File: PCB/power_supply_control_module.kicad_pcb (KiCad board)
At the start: 2 copper layers, 3 parts, among them SW3 RotaryEncoder, SW4 RotaryEncoder, U1 ATmega328P-A

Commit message: schematic and board WIP
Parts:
- added C1: 100nF, Capacitor_SMD:C_1206_3216Metric_Pad1.33x1.80mm_HandSolder, F.Cu at (142.0, 87.2)
- added C2: 1uF, Capacitor_SMD:C_1206_3216Metric_Pad1.33x1.80mm_HandSolder, F.Cu at (142.0, 84.8)
- added C3: 10uF, Capacitor_SMD:C_1206_3216Metric_Pad1.33x1.80mm_HandSolder, F.Cu at (142.0, 82.3)
- added C4: 22pF, Capacitor_SMD:C_1206_3216Metric_Pad1.33x1.80mm_HandSolder, F.Cu at (143.5, 104.2)
- added C5: 22pF, Capacitor_SMD:C_1206_3216Metric_Pad1.33x1.80mm_HandSolder, F.Cu at (137.7, 104.2)
- added D1: Voltage, LED_SMD:LED_0603_1608Metric_Pad1.05x0.95mm_HandSolder, B.Cu at (131.8, 108.3)
- added D2: Current, LED_SMD:LED_0603_1608Metric_Pad1.05x0.95mm_HandSolder, B.Cu at (175.8, 108.3)
- added H1: MountingHole, MountingHole:MountingHole_3.2mm_M3_ISO7380, F.Cu at (125.3, 98.8)
- added H2: MountingHole, MountingHole:MountingHole_3.2mm_M3_ISO7380, F.Cu at (181.9, 98.8)
- added J1: ICSP, Connector_PinHeader_2.54mm:PinHeader_2x03_P2.54mm_Vertical, F.Cu at (152.9, 92.0)
- added J2: PS_POT, Connector_JST:JST_XH_B4B-XH-A_1x04_P2.50mm_Vertical, F.Cu at (151.2, 79.3)
- added J3: PWR+UART, Connector_PinHeader_2.54mm:PinHeader_1x04_P2.54mm_Vertical, F.Cu at (126.5, 124.4)
- added R1: 10K, Resistor_SMD:R_1206_3216Metric_Pad1.30x1.75mm_HandSolder, F.Cu at (167.4, 108.0)
- added R2: 1K, Resistor_SMD:R_1206_3216Metric_Pad1.30x1.75mm_HandSolder, B.Cu at (127.0, 107.3)
- added R3: 1K, Resistor_SMD:R_1206_3216Metric_Pad1.30x1.75mm_HandSolder, B.Cu at (182.1, 107.8)
- added R4: 1K, Resistor_SMD:R_1206_3216Metric_Pad1.30x1.75mm_HandSolder, F.Cu at (143.4, 123.8)
- added R5: 1K, Resistor_SMD:R_1206_3216Metric_Pad1.30x1.75mm_HandSolder, F.Cu at (140.5, 123.8)
- added SW1: Voltage, Button_Switch_THT:SW_TH_Tactile_Omron_B3F-107x, B.Cu at (129.6, 110.2)
- added SW2: Current, Button_Switch_THT:SW_TH_Tactile_Omron_B3F-107x, B.Cu at (173.4, 110.2)
- added U2: MCP4251-103E-SL, Package_SO:SOIC-14_3.9x8.7mm_P1.27mm, F.Cu at (170.8, 100.2)
- added Y1: Crystal, Crystal:Crystal_HC49-4H_Vertical, B.Cu at (142.8, 101.2)
- SW3: value RotaryEncoder -> Voltage; moved to B.Cu
- SW4: value RotaryEncoder -> Current; moved to B.Cu
- moved SW4 63.4 mm to (173.2, 77.3), turned to -90 degrees
- moved U1 30.9 mm to (138.3, 94.0), turned to 90 degrees
- moved SW3 23.8 mm to (129.3, 77.3), turned to -90 degrees
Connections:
- SW3 pad A: unconnected-(SW3-PadA) -> /ENC_V_A
- SW3 pad B: unconnected-(SW3-PadB) -> /ENC_V_B
- SW3 pad C: unconnected-(SW3-PadC) -> GNDD
- SW4 pad A: unconnected-(SW4-PadA) -> /ENC_A_A
- SW4 pad B: unconnected-(SW4-PadB) -> /ENC_A_B
- SW4 pad C: unconnected-(SW4-PadC) -> GNDD
- U1 pad 1: unconnected-(U1-PD3-Pad1) -> /SW_A
- U1 pad 10: unconnected-(U1-PD6-Pad10) -> /ENC_A_A
- U1 pad 11: unconnected-(U1-PD7-Pad11) -> /ENC_A_B
- U1 pad 14: unconnected-(U1-PB2-Pad14) -> /~{MCP_CS}
- U1 pad 15: unconnected-(U1-PB3-Pad15) -> /MOSI
- U1 pad 16: unconnected-(U1-PB4-Pad16) -> /MISO
- U1 pad 17: unconnected-(U1-PB5-Pad17) -> /SCK
- U1 pad 18: unconnected-(U1-AVCC-Pad18) -> VCC
- U1 pad 2: unconnected-(U1-PD4-Pad2) -> /ENC_V_A
- U1 pad 21: Net-(U1-GND-Pad21) -> GNDD
- U1 pad 25: unconnected-(U1-PC2-Pad25) -> /LED_V
- U1 pad 26: unconnected-(U1-PC3-Pad26) -> /LED_A
- U1 pad 29: unconnected-(U1-~{RESET}/PC6-Pad29) -> /RST
- U1 pad 3: Net-(U1-GND-Pad21) -> GNDD
- U1 pad 30: unconnected-(U1-PD0-Pad30) -> /RXD0
- U1 pad 31: unconnected-(U1-PD1-Pad31) -> /TXD0
- U1 pad 32: unconnected-(U1-PD2-Pad32) -> /SW_V
- U1 pad 4: Net-(U1-VCC-Pad4) -> VCC
- U1 pad 5: Net-(U1-GND-Pad21) -> GNDD
- U1 pad 6: Net-(U1-VCC-Pad4) -> VCC
- U1 pad 7: unconnected-(U1-XTAL1/PB6-Pad7) -> Net-(U1-XTAL1/PB6)
- U1 pad 8: unconnected-(U1-XTAL2/PB7-Pad8) -> Net-(U1-XTAL2/PB7)
- U1 pad 9: unconnected-(U1-PD5-Pad9) -> /ENC_V_B
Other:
- board outline added: 64.3 x 55 mm

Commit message: second MCP added WIP
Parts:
- added R10: 10K, Resistor_SMD:R_1206_3216Metric_Pad1.30x1.75mm_HandSolder, F.Cu at (166.7, 124.4)
- added R11: 10K, Resistor_SMD:R_1206_3216Metric_Pad1.30x1.75mm_HandSolder, F.Cu at (166.7, 127.7)
- added R4: 2k, Resistor_SMD:R_1206_3216Metric_Pad1.30x1.75mm_HandSolder, F.Cu at (163.8, 108.0)
- added R7: 10K, Resistor_SMD:R_1206_3216Metric_Pad1.30x1.75mm_HandSolder, F.Cu at (165.2, 113.3)
- added R8: 10K, Resistor_SMD:R_1206_3216Metric_Pad1.30x1.75mm_HandSolder, F.Cu at (166.7, 117.8)
- added R9: 10K, Resistor_SMD:R_1206_3216Metric_Pad1.30x1.75mm_HandSolder, F.Cu at (166.7, 121.1)
- added U3: MCP4251-103E-SL, Package_SO:SOIC-14_3.9x8.7mm_P1.27mm, F.Cu at (177.8, 122.8)
- renumbered R4 to R5, R5 to R6
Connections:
- net /~{MCP_CS} renamed /~{MCP_CS1}
- U1 pad 13: unconnected-(U1-PB1-Pad13) -> /~{MCP_CS2}
- U2 pad 7: /_VCC -> Net-(U2-P1A)

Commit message: Schematic finished
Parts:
- added C4: 100nF, Capacitor_SMD:C_1206_3216Metric_Pad1.33x1.80mm_HandSolder, F.Cu at (171.7, 100.3)
- added C7: 100nF, Capacitor_SMD:C_1206_3216Metric_Pad1.33x1.80mm_HandSolder, F.Cu at (171.7, 103.7)
- moved R4 11.9 mm to (138.1, 111.5)
- moved R8 9.91 mm to (130.6, 124.2)
- moved R7 8.60 mm to (134.8, 123.8)
- moved U3 6.15 mm to (170.6, 94.1)
- moved J2 3.79 mm to (124.5, 121.2), turned to 180 degrees
- renumbered C4 to C5, C5 to C6, J3 to J2, J2 to J3, R7 to R1, R11 to R10, R10 to R11, R8 to R2, R4 to R3, R2 to R4, R3 to R5, R9 to R6, R5 to R7, R6 to R8, R1 to R9, U3 to U1, U1 to U2, U2 to U3
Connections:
- net /ENC_A_A renamed /ENC_C_A
- net /ENC_A_B renamed /ENC_C_B
- net /LED_A renamed /LED_C
- net /SW_A renamed /SW_C
- net /_POT_A renamed /_POT_C
- J3 pad 3: /_GND -> GND2
- J3 pad 4: /_VCC -> VCC2
- R1 pad 1: /~{MCP_CS1} -> /~{MCP_CS2}
- R10 pad 1: unconnected-(R11-Pad1) -> Net-(U1-P0B)
- R10 pad 2: unconnected-(R11-Pad2) -> GND2
- R11 pad 1: unconnected-(R10-Pad1) -> GND2
- R11 pad 2: unconnected-(R10-Pad2) -> Net-(U1-P1B)
- R2 pad 1: unconnected-(R8-Pad1) -> Net-(U1-P0B)
- R2 pad 2: unconnected-(R8-Pad2) -> VCC2
- R3 pad 1: /_VCC -> VCC2
- R3 pad 2: Net-(U2-P1A) -> Net-(U1-P1A)
- R6 pad 1: unconnected-(R9-Pad1) -> Net-(U1-P1B)
- R6 pad 2: unconnected-(R9-Pad2) -> Net-(U1-P1A)
- U1 pad 1: /~{MCP_CS1} -> /~{MCP_CS2}
- U1 pad 10: unconnected-(U3-P0B-Pad10) -> Net-(U1-P0B)
- U1 pad 5: unconnected-(U3-P1B-Pad5) -> Net-(U1-P1B)
- U1 pad 6: unconnected-(U3-P1W-Pad6) -> Net-(U1-P1B)
- U1 pad 7: unconnected-(U3-P1A-Pad7) -> Net-(U1-P1A)
- U1 pad 8: unconnected-(U3-P0A-Pad8) -> VCC2
- U1 pad 9: unconnected-(U3-P0W-Pad9) -> Net-(U1-P0B)
- U3 pad 10: /_GND -> GND2
- U3 pad 5: /_GND -> GND2
- U3 pad 7: Net-(U2-P1A) -> Net-(U1-P1B)
- U3 pad 8: /_VCC -> Net-(U1-P0B)

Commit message: PCB WIP
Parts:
- R4: moved to F.Cu
- moved R10 24.0 mm to (173.8, 104.8), turned to 180 degrees
- moved R6 21.4 mm to (152.8, 104.8)
- moved R3 21.2 mm to (183.5, 115.8)
- moved C7 20.9 mm to (175.7, 124.2), turned to 90 degrees
- moved R7 20.2 mm to (123.3, 107.2), turned to -90 degrees
- moved R9 18.7 mm to (173.7, 90.4), turned to 0 degrees
- moved R11 18.6 mm to (173.8, 107.2), turned to 180 degrees
- moved R8 17.4 mm to (126.5, 107.2)
- moved R1 17.0 mm to (178.4, 124.2), turned to -90 degrees
- moved R2 15.8 mm to (152.4, 111.0)
- moved C2 8.97 mm to (133.7, 88.2), turned to 180 degrees
- moved U1 8.36 mm to (169.5, 124.0), turned to -90 degrees
- moved C4 7.64 mm to (173.7, 92.9), turned to 180 degrees
- moved J1 6.23 mm to (147.8, 88.5)
- moved U3 5.71 mm to (173.7, 98.9), turned to 0 degrees
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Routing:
- net /MISO: track 0.00 -> 78.1 mm, vias 0 -> 3
- net /ENC_C_B: track 0.00 -> 67.8 mm, vias 0 -> 1
- net /SCK: track 0.00 -> 67.6 mm, vias 0 -> 3
- net /MOSI: track 0.00 -> 65.9 mm
- net /ENC_C_A: track 0.00 -> 64.5 mm, vias 0 -> 1
- net /LED_V: track 0.00 -> 57.7 mm, vias 0 -> 2
- net VCC: track 0.00 -> 56.4 mm
- net /RST: track 0.00 -> 43.5 mm
- net /ENC_V_B: track 0.00 -> 28.5 mm, vias 0 -> 2
- net /SW_C: track 0.00 -> 26.9 mm, vias 0 -> 1
- net GND2: track 0.00 -> 25.8 mm
- net /LED_C: track 0.00 -> 24.1 mm, vias 0 -> 1
- net /ENC_V_A: track 0.00 -> 23.5 mm, vias 0 -> 2
- net GNDD: track 0.00 -> 23.3 mm, vias 0 -> 9
- net /SW_V: track 0.00 -> 22.9 mm, vias 0 -> 1
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- added copper zone on In1.Cu, net GNDD
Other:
- outline, holes or cut-outs redrawn
- copper layers 2 -> 4

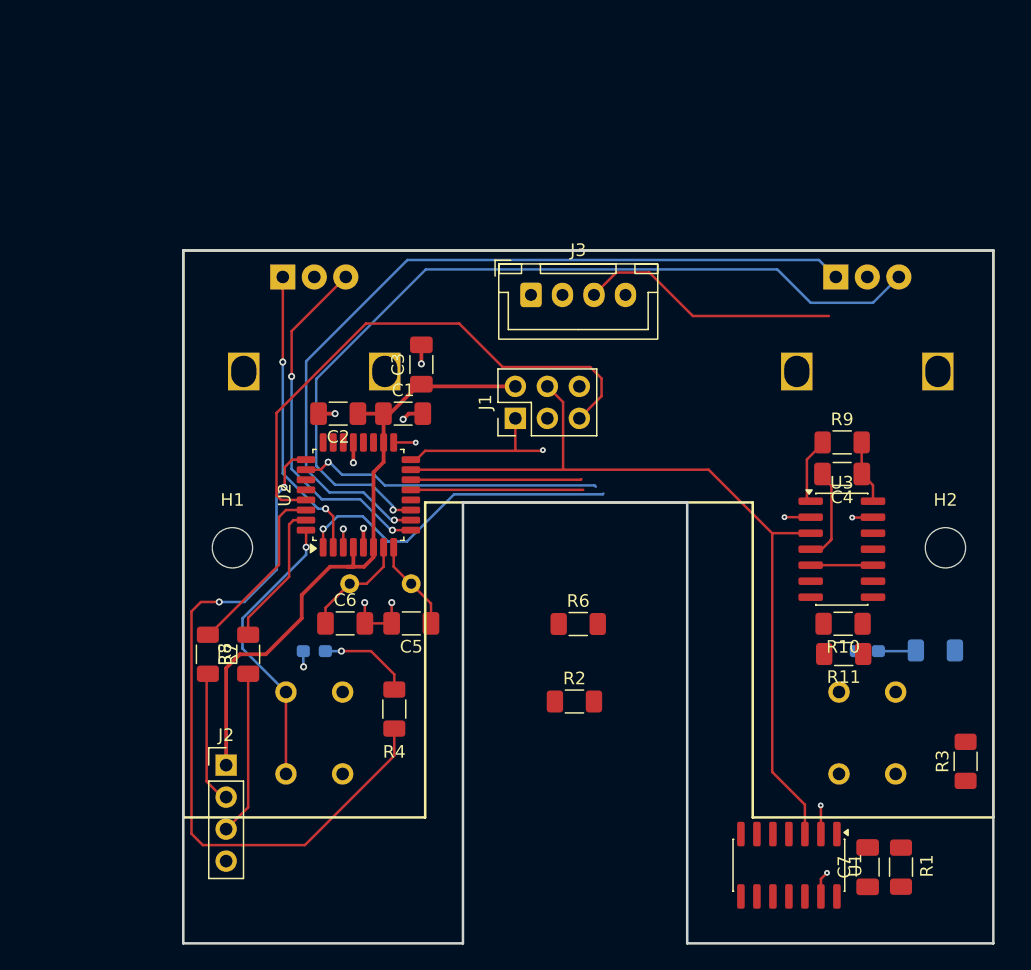
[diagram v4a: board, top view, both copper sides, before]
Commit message: added USB PCB, before connecting the PCBs
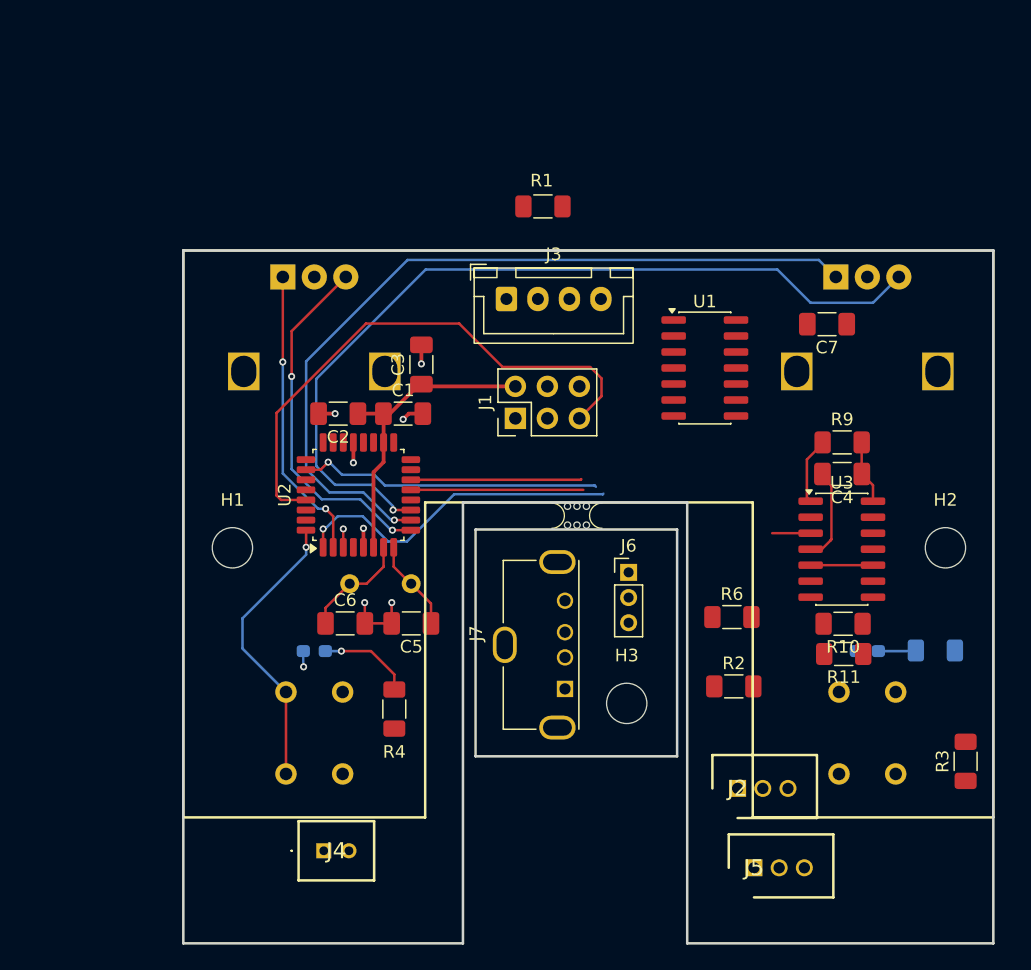
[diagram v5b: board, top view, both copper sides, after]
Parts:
- removed R7, R8: 1K, Resistor_SMD:R_1206_3216Metric_Pad1.30x1.75mm_HandSolder
- added B1: MouseBite, lib:mouse-bite-2mm-slot, F.Cu at (152.7, 96.2)
- added H3: MountingHole, MountingHole:MountingHole_3.2mm_M3_ISO7380, F.Cu at (156.6, 111.2)
- added J4: POWER, EDAC:140502415001, F.Cu at (132.6, 122.8)
- added J5: Display, EDAC:SHDR3W50P0X200_1X3_800X470X640P, F.Cu at (166.7, 124.2)
- added J6: USB_Y, Connector_PinHeader_2.00mm:PinHeader_1x03_P2.00mm_Vertical, F.Cu at (156.8, 100.8)
- added J7: USB_A, Connector_USB:USB_A_Molex_105057_Vertical, F.Cu at (151.7, 110.0)
- J2: value PWR+UART -> USB_X; footprint Connector_PinHeader_2.54mm:PinHeader_1x04_P2.54mm_Vertical -> EDAC:SHDR3W50P0X200_1X3_800X470X640P
- moved R1 59.7 mm to (149.9, 71.7), turned to 0 degrees
- moved C7 43.2 mm to (172.5, 81.0), turned to 180 degrees
- moved J2 40.6 mm to (165.4, 117.9)
- moved U1 40.0 mm to (162.8, 84.5), turned to 0 degrees
- moved R2 12.7 mm to (165.1, 109.8)
- moved R6 12.2 mm to (164.9, 104.3)
- moved J3 1.98 mm to (147.1, 79.0)
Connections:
- J2 pad 1: VCC -> /RXD0
- J2 pad 2: Net-(J2-Pin_2) -> /TXD0
- J2 pad 3: Net-(J2-Pin_3) -> GNDD
- U2 pad 1: /SW_C -> /DIN
- U2 pad 27: unconnected-(U2-PC4-Pad27) -> /SW_V
- U2 pad 28: unconnected-(U2-PC5-Pad28) -> /SW_C
- U2 pad 32: /SW_V -> /CLK
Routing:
- net /MISO: track 78.1 -> 0.00 mm, vias 3 -> 0
- net /SCK: track 67.6 -> 0.02 mm, vias 3 -> 0
- net /MOSI: track 65.9 -> 3.05 mm
- net /LED_V: track 57.7 -> 0.00 mm, vias 2 -> 0
- net VCC: track 56.4 -> 29.5 mm
- net /SW_C: track 26.9 -> 0.00 mm, vias 1 -> 0
- net /DIN: track 0.00 -> 26.9 mm, vias 0 -> 1
- net GND2: track 25.8 -> 4.95 mm
- net /RXD0: track 14.2 -> 0.00 mm
- net Net-(J2-Pin_3): track 13.1 -> 0.00 mm
- net /TXD0: track 11.6 -> 0.00 mm
- net Net-(J2-Pin_2): track 10.7 -> 0.00 mm
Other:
- outline, holes or cut-outs redrawn

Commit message: USB PCB finished
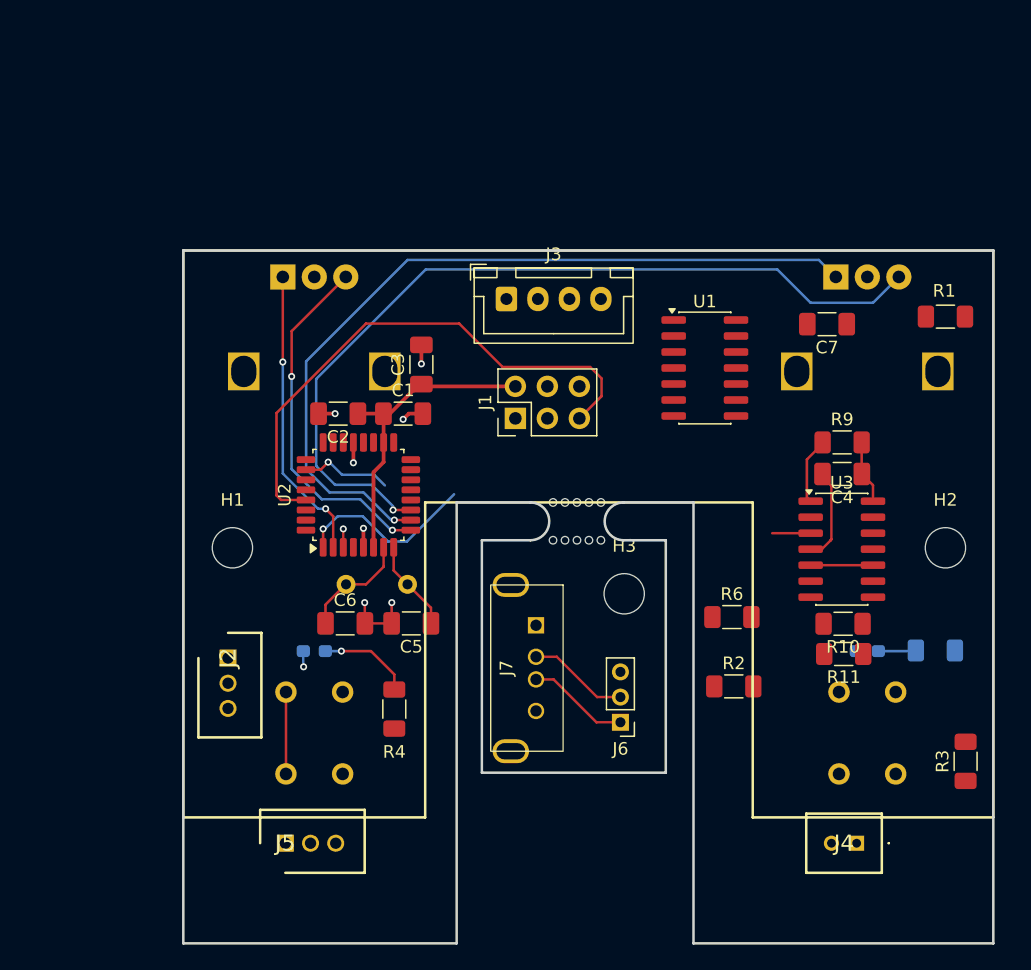
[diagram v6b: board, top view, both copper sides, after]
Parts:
- B1: footprint lib:mouse-bite-2mm-slot -> lib:mouse-bite-3mm-slot-jlcpcb
- J7: footprint Connector_USB:USB_A_Molex_105057_Vertical -> USB_A:USB_A_Molex_105057_Vertical
- moved J4 42.3 mm to (174.8, 122.2), turned to 180 degrees
- moved J2 41.8 mm to (125.0, 107.5), turned to -90 degrees
- moved J5 37.3 mm to (129.5, 122.2)
- moved R1 33.1 mm to (181.9, 80.5)
- moved J6 11.9 mm to (156.1, 112.7), turned to 180 degrees
- moved H3 8.70 mm to (156.4, 102.5)
- moved J7 2.83 mm to (149.4, 108.3), turned to -90 degrees
- moved B1 0.45 mm to (152.7, 96.7)
- moved Y1 0.29 mm to (139.2, 101.7)
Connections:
- net Net-(J6-Pin_1) renamed /D+
- net Net-(J6-Pin_2) renamed /D-
- net Net-(J6-Pin_3) renamed /GND_USB
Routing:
- net /LED_C: track 24.1 -> 7.28 mm
- net /SW_V: track 22.9 -> 6.50 mm, vias 1 -> 0
- net /~{MCP_CS2}: track 13.7 -> 0.00 mm
- net /~{MCP_CS1}: track 18.9 -> 5.31 mm
- net /DIN: track 26.9 -> 15.0 mm
- net /D+: track 0.00 -> 8.11 mm
- net /D-: track 0.00 -> 8.03 mm
- added copper zone on In1.Cu, net /GND_USB
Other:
- outline, holes or cut-outs redrawn

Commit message: routing finished
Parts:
- moved R2 23.6 mm to (180.3, 91.8), turned to 90 degrees
- moved R3 20.8 mm to (166.2, 104.2), turned to 180 degrees
- moved R1 11.5 mm to (170.4, 80.5)
- moved C7 9.86 mm to (162.9, 78.6)
- moved R6 2.62 mm to (166.2, 106.6), turned to 180 degrees
- moved R9 0.88 mm to (173.7, 89.5)
- moved R10 0.83 mm to (174.6, 104.8)
- moved R11 0.78 mm to (174.6, 107.2)
- moved J5 0.51 mm to (130.0, 122.3)
- moved J4 0.30 mm to (174.8, 122.0)
- moved U1 0.07 mm to (162.8, 84.5)
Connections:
- U2 pad 13: /~{MCP_CS2} -> /~{MCP_CS1}
- U2 pad 14: /~{MCP_CS1} -> /~{MCP_CS2}
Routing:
- net VCC: track 29.5 -> 108.7 mm, vias 0 -> 3
- net /SW_C: track 0.00 -> 66.3 mm, vias 0 -> 1
- net /LED_C: track 7.28 -> 73.2 mm
- net VCC2: track 0.00 -> 56.1 mm, vias 0 -> 3
- net /SCK: track 0.02 -> 54.1 mm, vias 0 -> 4
- net /MISO: track 0.00 -> 53.1 mm, vias 0 -> 3
- net /MOSI: track 3.05 -> 54.8 mm
- net /~{MCP_CS2}: track 0.00 -> 49.5 mm, vias 0 -> 2
- net /_POT_C: track 0.00 -> 43.6 mm, vias 0 -> 1
- net GND2: track 4.95 -> 46.5 mm, vias 0 -> 1
- net Net-(U1-P0B): track 0.00 -> 37.6 mm
- net Net-(U1-P1B): track 0.00 -> 36.6 mm, vias 0 -> 2
- net /_POT_V: track 0.00 -> 36.3 mm, vias 0 -> 1
- net /LED_V: track 0.00 -> 33.4 mm, vias 0 -> 2
- net /~{MCP_CS1}: track 5.31 -> 38.3 mm, vias 0 -> 2
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- added copper zone on B.Cu, net /GND_USB
- added copper zone on F.Cu, net /GND_USB
- added copper zone on B.Cu, net GNDD
- added copper zone on F.Cu, net GNDD
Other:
- board size 64.3 x 55 mm -> 64.3 x 50.3 mm

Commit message: PCB finished, JLCPCB ordered
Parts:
- J5: value Display -> DISP
- U2: value ATmega328P-A -> ATmega328PB-A
- moved J4 6.97 mm to (167.9, 121.4)
- moved R5 2.10 mm to (181.8, 109.0), turned to -90 degrees
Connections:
- net /CLK renamed /DISP_CLK
- net /DIN renamed /DISP_DIN
- SW3 pad MP: (no net) -> GNDD
- SW4 pad MP: (no net) -> GNDD
- U2 pad 3: GNDD -> unconnected-(U2-PE0-Pad3)
- U2 pad 6: VCC -> unconnected-(U2-PE1-Pad6)
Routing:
- net /LED_C: track 73.2 -> 68.1 mm
- net VCC: track 108.7 -> 113.1 mm
- net /RST: track 46.7 -> 49.1 mm
- net Net-(D2-A): track 3.00 -> 5.34 mm
- net /SW_C: track 66.3 -> 64.7 mm
- net GNDD: track 32.5 -> 31.1 mm, vias 28 -> 30
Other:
- board text added: "+5V"
- board text added: "2026-01-29"
- board text added: "CLK"
- board text added: "DIN"
- board text added: "Designed by MT"
- board text added: "GND"
- board text added: "JLCJLCJLCJLC"
- board text added: "RX"
- board text added: "TX"
- board text added: "USB"
- board text added: "v1.0.0"
